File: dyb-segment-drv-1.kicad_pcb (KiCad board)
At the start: 2 copper layers, 10 x 3 mm, 187 parts, among them J1 Conn_01x10, Q1 HL2300, Q10 HL2300, Q11 HL2300, Q12 HL2300, Q13 HL2300, Q14 HL2300, Q15 HL2300, Q16 HL2300, Q2 HL2300, Q3 HL2300, Q4 HL2300, Q5 HL2300, Q6 HL2300, Q7 HL2300, Q8 HL2300, Q9 HL2300, SW1 SW_SPDT, U1 AP2112K-1.8, U10 74AUC2G32, U11 74AUC2G32, U12 74AUC2G32, U13 74AUC2G32, U14 74AUC2G32, U15 Inverter_Schmitt_Dual, U16 Inverter_Schmitt_Dual, U17 SN74AUP2G08, U18 SN74AUP2G08, U19 SN74AUP2G08, U2 GS3911AG, U20 SN74AUP2G08, U21 SN74AUP2G08, U22 74AUC2G32, U23 74AUC2G32, U24 74AUC2G32, U25 74AUC2G32, U26 74AUC2G32, U27 GS3911AG, U28 SN74AUP2G08, U29 SN74AUP2G08, U3 SN74AUP2G08, U30 SN74AUP2G08, U31 SN74AUP2G08, U32 SN74AUP2G08, U33 SN74AUP2G08, U34 74AUC2G32, U35 74AUC2G32, U36 74AUC2G32, U37 74AUC2G32, U38 74AUC2G32, U39 74AUC2G32, U4 SN74AUP2G08, U40 Inverter_Schmitt_Dual, U41 Inverter_Schmitt_Dual, U42 SN74AUP2G08, U43 SN74AUP2G08, U44 SN74AUP2G08, U45 SN74AUP2G08, U46 SN74AUP2G08, U47 74AUC2G32, U48 74AUC2G32, U49 74AUC2G32, U5 SN74AUP2G08, U50 74AUC2G32, U51 74AUC2G32, U6 SN74AUP2G08, U7 SN74AUP2G08, U8 SN74AUP2G08, U9 74AUC2G32

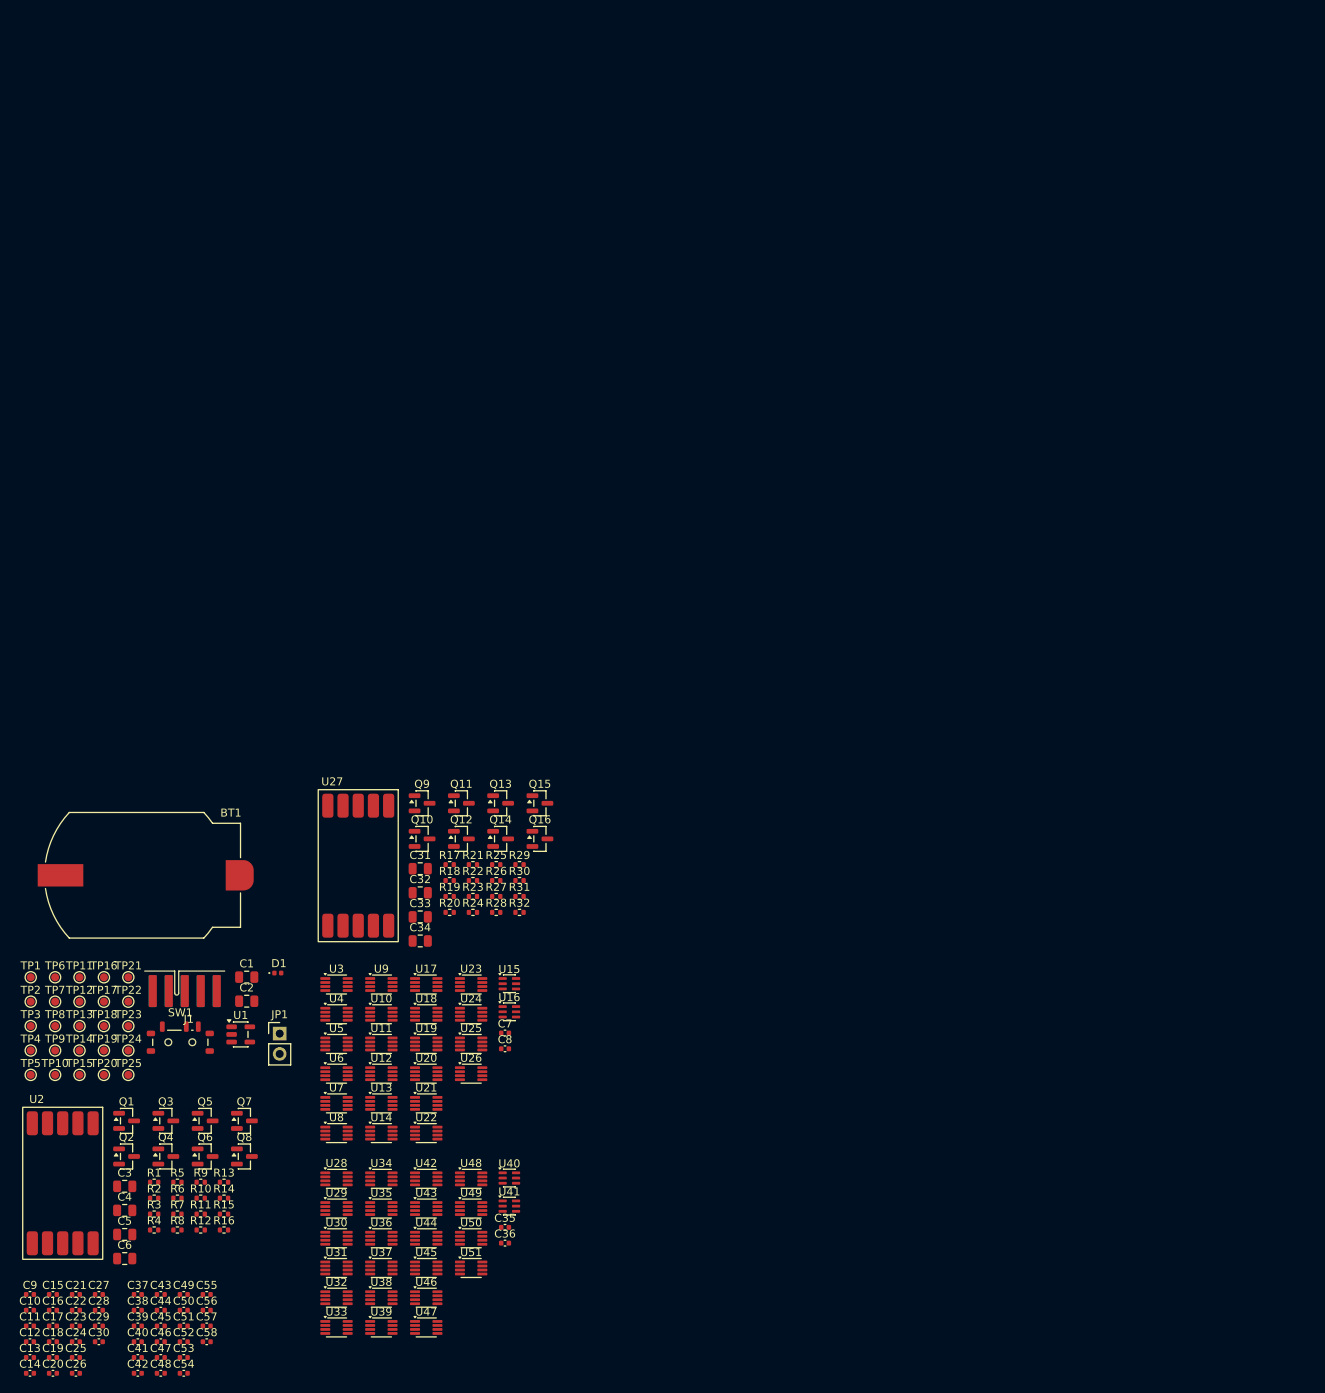
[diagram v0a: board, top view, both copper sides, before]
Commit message: pcb: initial driver gates placement
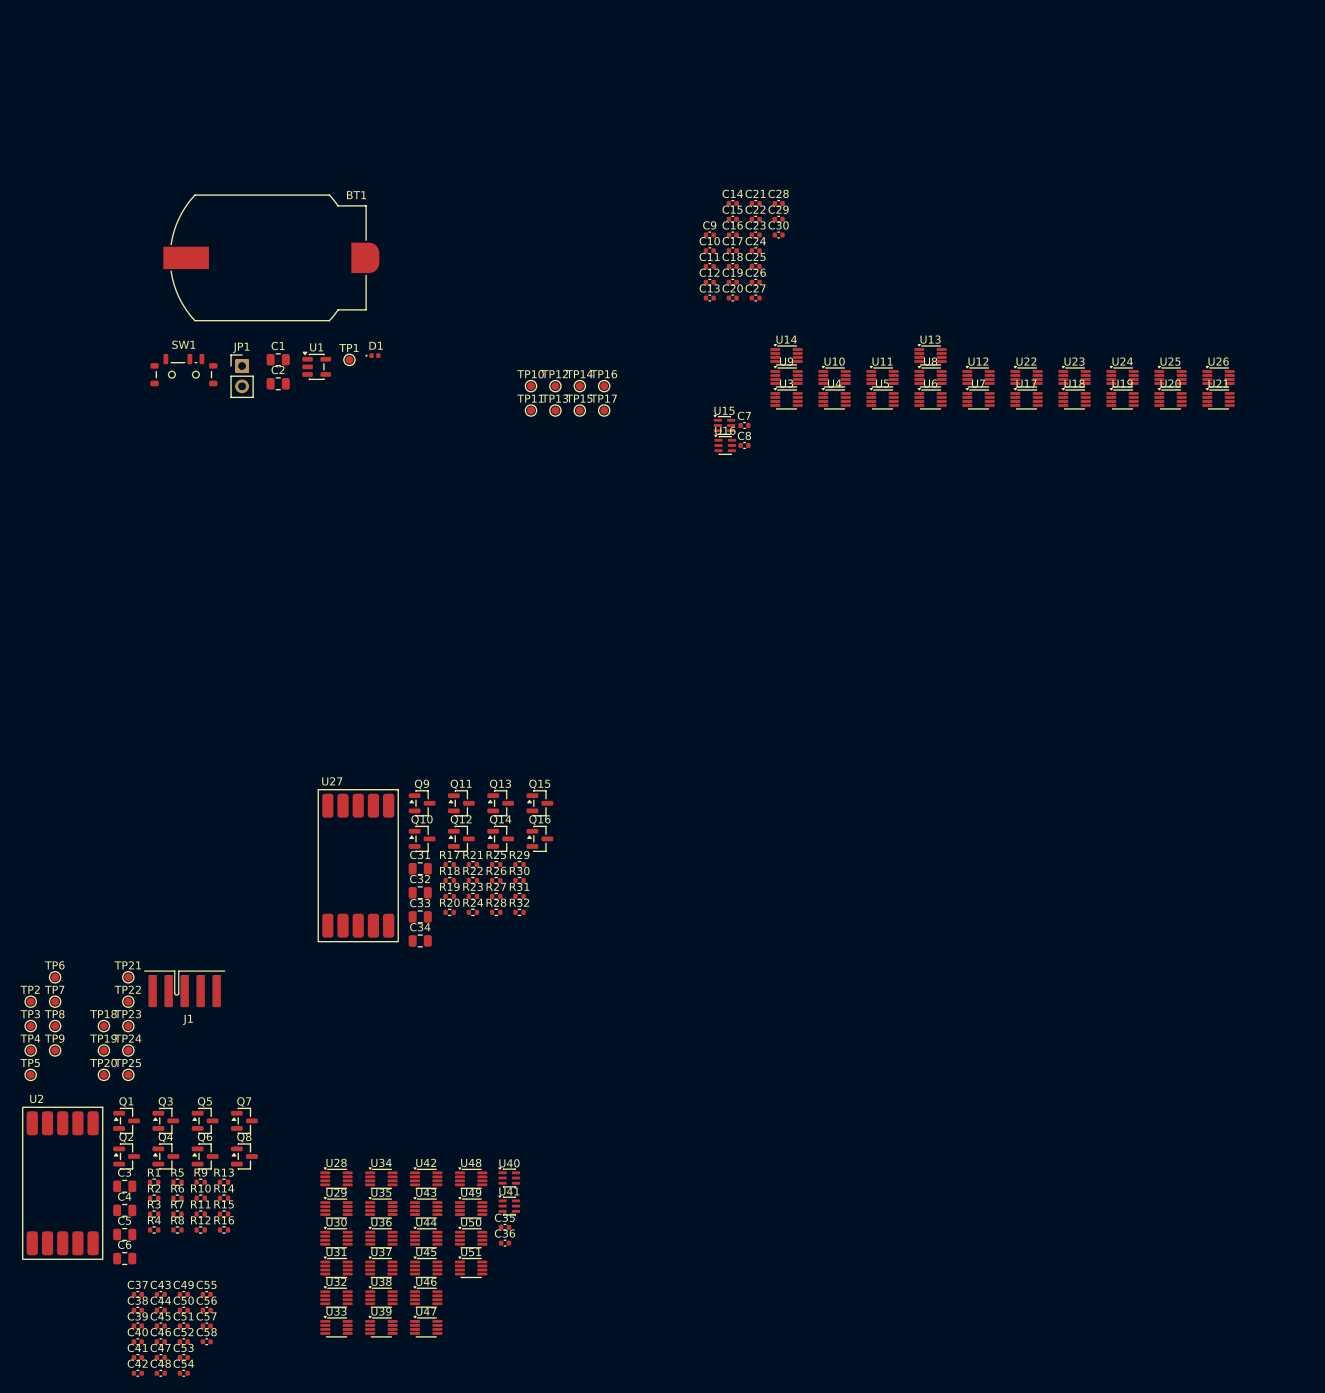
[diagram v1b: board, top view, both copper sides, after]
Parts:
- moved C14 170.6 mm to (114.0, 42.2)
- moved C28 162.4 mm to (119.8, 42.2)
- moved C29 162.4 mm to (119.8, 44.2)
- moved C30 162.4 mm to (119.8, 46.2)
- moved C21 160.7 mm to (116.9, 42.2)
- moved C22 160.7 mm to (116.9, 44.2)
- moved C23 160.7 mm to (116.9, 46.2)
- moved C24 160.7 mm to (116.9, 48.2)
- moved C25 160.7 mm to (116.9, 50.1)
- moved C26 160.7 mm to (116.9, 52.1)
- moved C15 159.0 mm to (114.0, 44.2)
- moved C16 159.0 mm to (114.0, 46.2)
- moved C17 159.0 mm to (114.0, 48.2)
- moved C18 159.0 mm to (114.0, 50.1)
- moved C19 159.0 mm to (114.0, 52.1)
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
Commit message: pcb: add logic gates placement
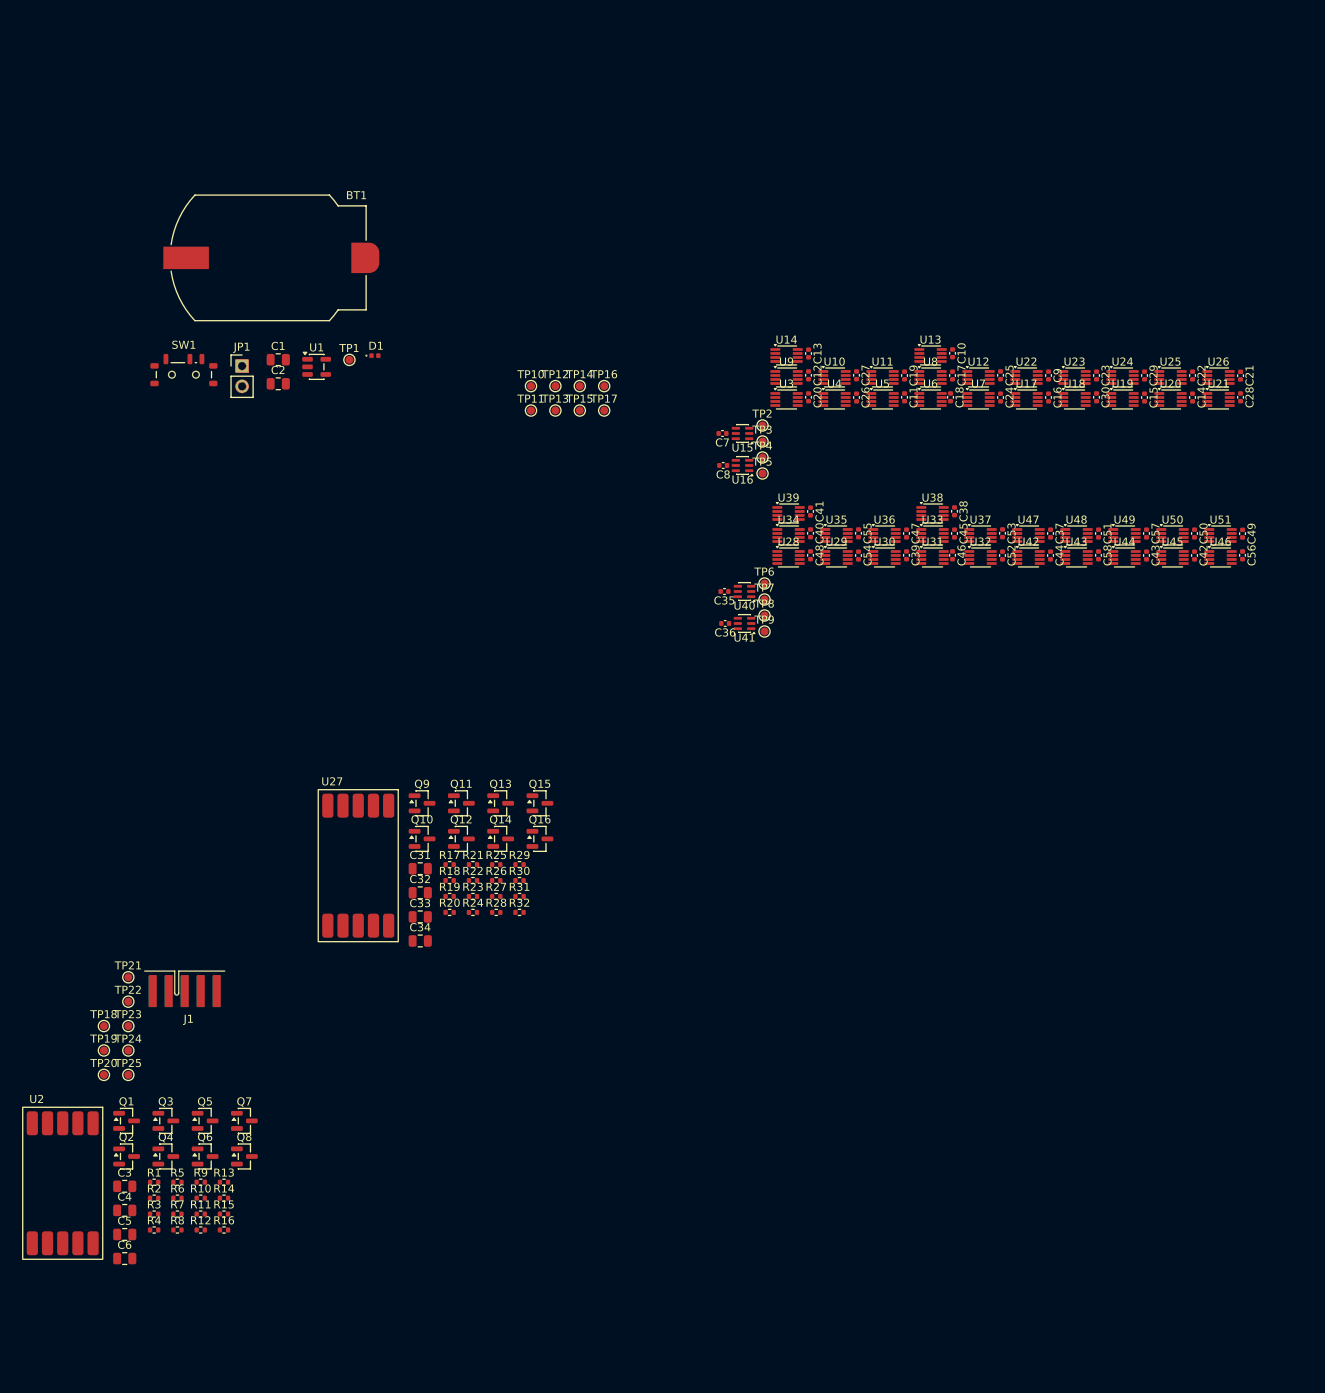
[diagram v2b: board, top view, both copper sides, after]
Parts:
- moved C42 167.0 mm to (171.8, 86.2), turned to -90 degrees
- moved C49 163.0 mm to (177.8, 83.5), turned to -90 degrees
- moved C56 160.2 mm to (177.8, 86.2), turned to -90 degrees
- moved C50 159.3 mm to (171.8, 83.5), turned to -90 degrees
- moved C43 154.0 mm to (165.8, 86.2), turned to -90 degrees
- moved C57 153.7 mm to (165.8, 83.5), turned to -90 degrees
- moved C51 151.3 mm to (159.8, 83.5), turned to -90 degrees
- moved C58 148.6 mm to (159.8, 86.2), turned to -90 degrees
- moved C37 148.5 mm to (153.8, 83.5), turned to -90 degrees
- moved C44 145.8 mm to (153.8, 86.2), turned to -90 degrees
- moved C53 145.2 mm to (147.8, 83.5), turned to -90 degrees
- moved C38 142.8 mm to (141.8, 80.7), turned to -90 degrees
- moved C52 141.9 mm to (147.8, 86.2), turned to -90 degrees
- moved C45 140.2 mm to (141.8, 83.5), turned to -90 degrees
- moved C46 139.5 mm to (141.5, 86.2), turned to -90 degrees
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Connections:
- U15 pad 1: /A0 -> /A1
- U15 pad 3: /A1 -> /A0
- U15 pad 4: /Segment Driver/~{D1} -> /Segment Driver/~{D0}
- U15 pad 6: /Segment Driver/~{D0} -> /Segment Driver/~{D1}
- U16 pad 1: /A2 -> /A3
- U16 pad 3: /A3 -> /A2
- U16 pad 4: /Segment Driver/~{D3} -> /Segment Driver/~{D2}
- U16 pad 6: /Segment Driver/~{D2} -> /Segment Driver/~{D3}
- U40 pad 1: /B0 -> /B1
- U40 pad 3: /B1 -> /B0
- U40 pad 4: /Segment Driver1/~{D1} -> /Segment Driver1/~{D0}
- U40 pad 6: /Segment Driver1/~{D0} -> /Segment Driver1/~{D1}
- U41 pad 1: /B2 -> /B3
- U41 pad 3: /B3 -> /B2
- U41 pad 4: /Segment Driver1/~{D3} -> /Segment Driver1/~{D2}
- U41 pad 6: /Segment Driver1/~{D2} -> /Segment Driver1/~{D3}

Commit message: pcb: add segment displays layout
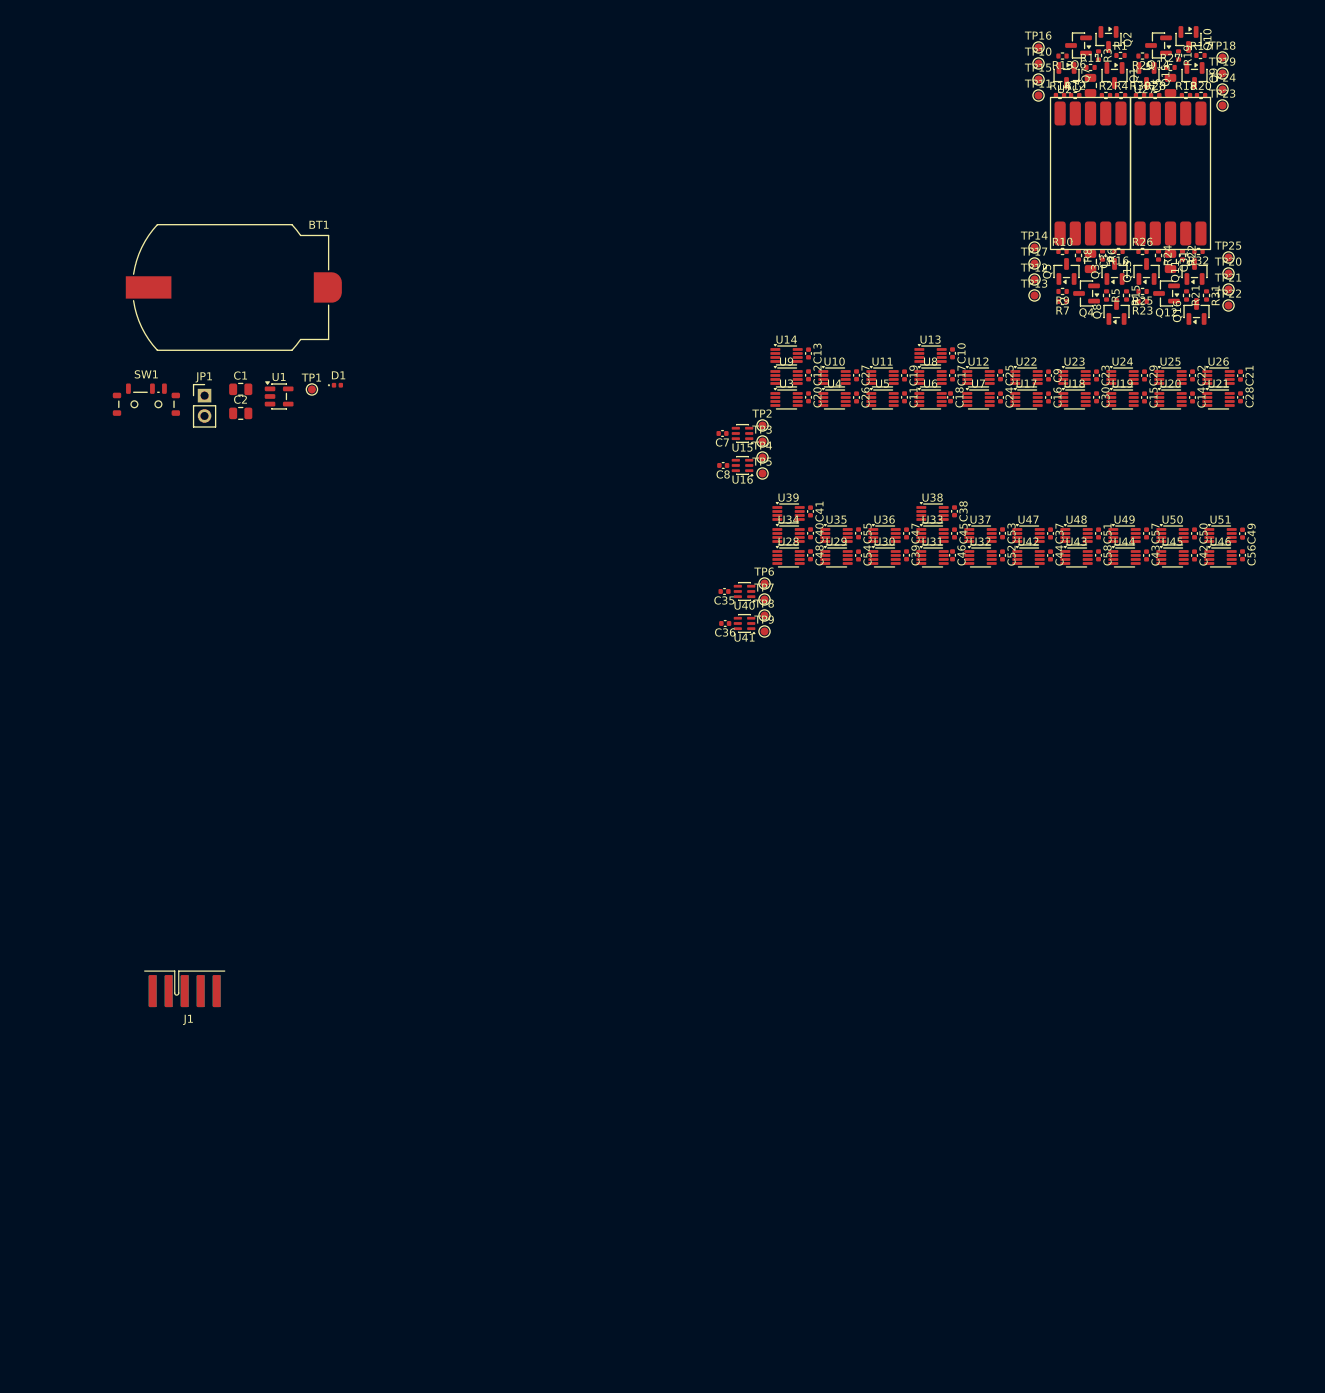
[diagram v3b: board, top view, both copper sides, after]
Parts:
- removed C32, C33, C34, C6: 10u, Capacitor_SMD:C_0805_2012Metric
- moved C5 194.2 mm to (168.8, 27.5), turned to 90 degrees
- moved R3 186.8 mm to (159.8, 23.8), turned to -90 degrees
- moved R4 186.3 mm to (162.6, 28.8)
- moved Q2 185.9 mm to (161.0, 21.8), turned to -90 degrees
- moved TP19 185.6 mm to (175.2, 26.0)
- moved R1 185.5 mm to (162.5, 23.8)
- moved C4 185.3 mm to (158.8, 27.5), turned to 90 degrees
- moved TP18 185.0 mm to (175.2, 24.0)
- moved R2 182.1 mm to (160.7, 28.7)
- moved TP24 182.0 mm to (175.2, 28.0)
- moved R11 181.4 mm to (158.8, 25.2)
- moved U2 180.1 mm to (158.8, 41.8)
- moved Q1 179.8 mm to (161.8, 26.2), turned to -90 degrees
- moved R12 179.1 mm to (156.8, 28.7)
- moved TP23 178.7 mm to (175.2, 30.0)
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
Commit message: pcb: add pwr layout
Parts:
- JP1: footprint Connector_PinHeader_2.54mm:PinHeader_1x02_P2.54mm_Vertical -> Connector_PinHeader_2.54mm:PinHeader_1x02_P2.54mm_Horizontal
- moved SW1 97.9 mm to (128.0, 23.0), turned to 180 degrees
- moved BT1 86.0 mm to (135.8, 41.5), turned to 90 degrees
- moved JP1 81.0 mm to (122.2, 34.0), turned to -90 degrees
- moved D1 78.5 mm to (132.5, 25.5)
- moved C1 70.7 mm to (116.2, 34.8), turned to -90 degrees
- moved C2 68.1 mm to (113.5, 38.2), turned to 180 degrees
- moved U1 64.3 mm to (113.5, 35.0), turned to -90 degrees
- moved TP1 58.7 mm to (114.5, 40.5)
